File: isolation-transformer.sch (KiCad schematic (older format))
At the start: 0 parts

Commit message: Final schematic version
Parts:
- added CB1: 15A 250V, symbol Device:CircuitBreaker_1P
- added F1: 100°C, symbol Device:Fuse
- added FL1: JRT0406-2, symbol CustomParts:EMI_Filter_LL_CCC
- added J11: IEC 60320 C20, symbol Connector:Conn_01x03_Female
- added J12: CEE 7/3 Schuko, symbol Connector:Conn_01x03_Female
- added J13, J14: NEMA 5-15R, symbol Connector:Conn_01x03_Female
- added NE1, NE2, NE3: Lamp_Neon, symbol Device:Lamp_Neon
- added PS1: 12V 330mA, symbol Converter_ACDC:HLK-PM12
- added R14: 300R 200W, symbol Device:R
- added R15, R16, R17: 150K, symbol Device:R
- added SW1: 15A 250V, symbol CustomParts:SW_DPDT_x2_MSM
- added SW2, SW3: 6A 250V, symbol Switch:SW_SPST
- added TR1: 2600 VA, symbol Transformer:TRANSF6
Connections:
- new net: F1.2, TR1.2
- new net: F1.1, TR1.3
- new net: FL1.1, J11.3 (Pin_3), TR1.4
- new net: CB1.1, J11.1 (Pin_1)
- new net: CB1.2, SW1.2 (B), SW1.5 (B)
- new net: NE1.1, R15.1
- new net: FL1.3, PS1.1 (AC/L)
- new net: FL1.4, PS1.2 (AC/N)
- new net: FL1.2, SW1.4 (A)
- new net: J12.2 (Pin_2), J13.2 (Pin_2), J14.2 (Pin_2), SW3.1 (A)
- new net: NE2.1, R16.1
- new net: NE3.1, R17.1
- new net +12V: PS1.4 (+Vout)
- new net GND: FL1.5, J11.2 (Pin_2), PS1.3 (-Vout), SW2.2 (B), SW3.2 (B)
- new net Mode Selection/115V_1_L: J13.1 (Pin_1), NE2.2
- new net Mode Selection/115V_1_N: J13.3 (Pin_3), R16.2
- new net Mode Selection/115V_2_L: J14.1 (Pin_1), NE3.2
- new net Mode Selection/115V_2_N: J14.3 (Pin_3), R17.2
- new net Mode Selection/230V_L: J12.1 (Pin_1), NE1.2
- new net Mode Selection/230V_N: J12.3 (Pin_3), R15.2
- new net Mode Selection/MODE_SW: SW2.1 (A)
- new net Mode Selection/W5: TR1.5
- new net Mode Selection/W6: TR1.6
- new net Mode Selection/W7: TR1.7
- new net Mode Selection/W8: TR1.8
- new net Soft Start/BALLAST_1: R14.2
- new net Soft Start/BALLAST_2: R14.1
- new net Soft Start/PWR_1: SW1.1 (A)
- new net Soft Start/PWR_2: SW1.3 (C), TR1.1
- no-connect marks 0 -> 1
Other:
- note added: "Connect/disconnect\nprotective earth"
- note added: "Fuse TC-coupled to\nthe side of transformer"
- note added: "Goes to Soft Start\nand Mode Selection"
- note added: "In direct mode without\npower 230V mode is default"
- note added: "Toggle between\n230V/115V modes"
- note added: "Toggle between\nsoft-start/direct modes"

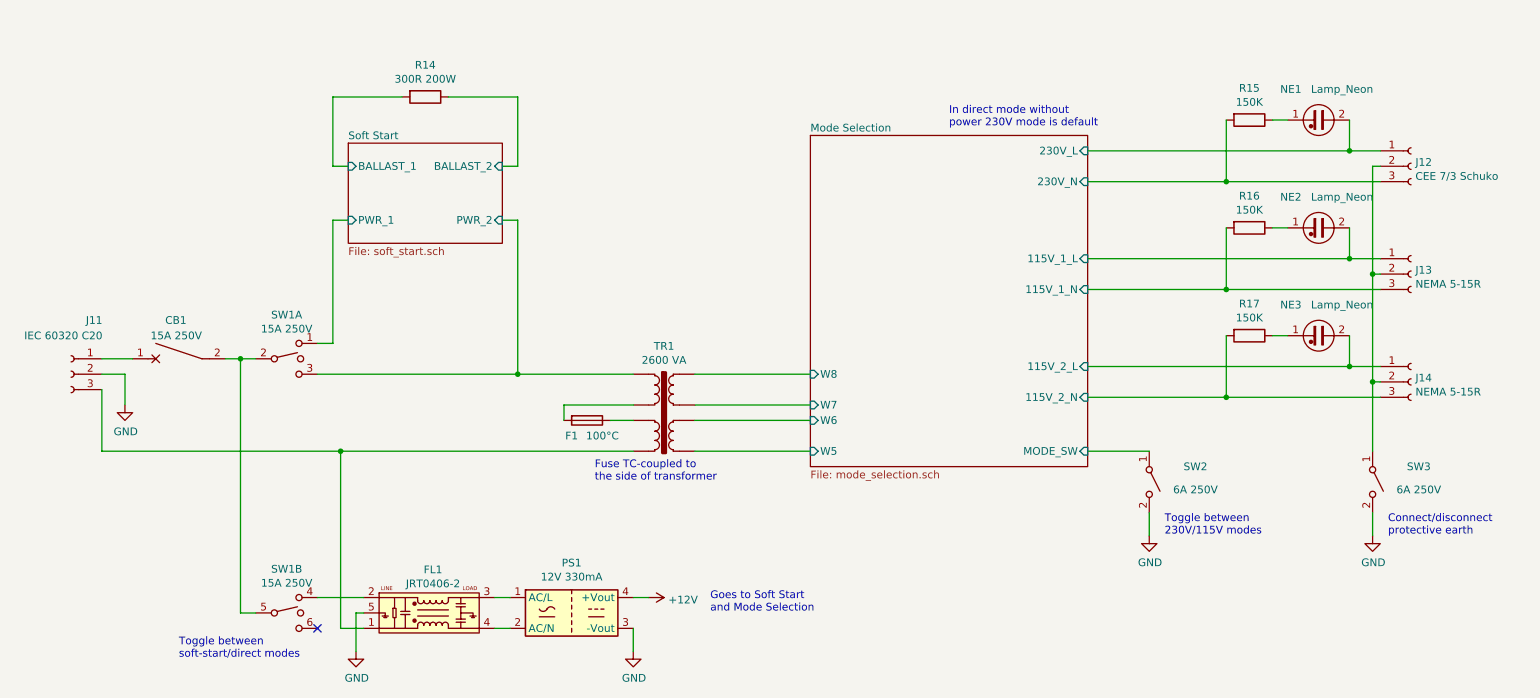
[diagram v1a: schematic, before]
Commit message: Actually used parts instead of generic ones
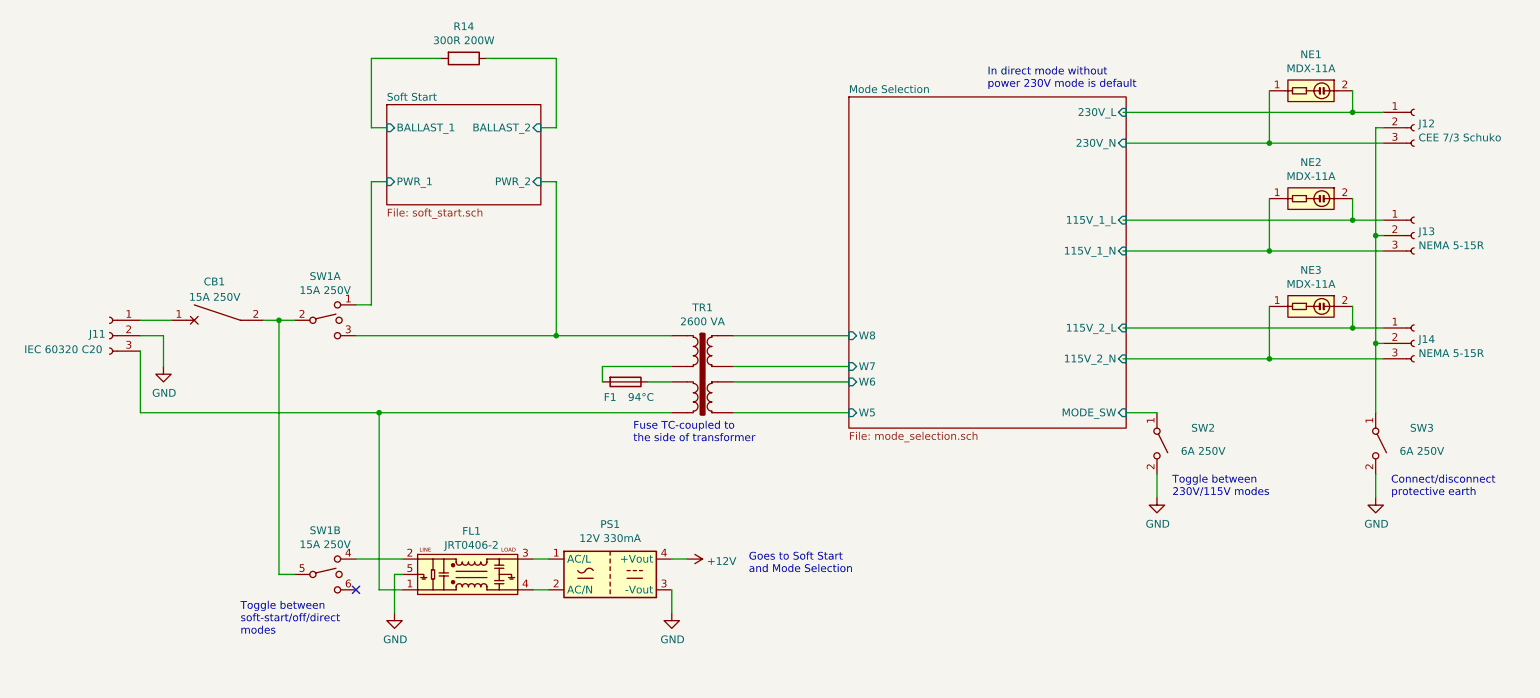
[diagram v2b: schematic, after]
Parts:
- removed NE1, NE2, NE3: Lamp_Neon, symbol Device:Lamp_Neon
- removed R15, R16, R17: 150K, symbol Device:R
- added NE1, NE2, NE3: MDX-11A, symbol CustomParts:Neon_Indicator
- F1: value 100°C -> 94°C
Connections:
- wire segments 69 -> 66
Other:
- note added: "Toggle between\nsoft-start/off/direct\nmodes"
- note removed: "Toggle between\nsoft-start/direct modes"
- moved on the sheet: CB1, F1, FL1, J11, J12, J13, J14, PS1, R14, SW1A, SW1B, SW2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

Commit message: Readme corrections, photos
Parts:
- added F1: 94°C, symbol Device:Fuse
- renumbered F1 to F2
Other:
- note added: "Fuses TC-coupled to\nthe sides of transformer"
- note removed: "Fuse TC-coupled to\nthe side of transformer"
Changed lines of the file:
@@
 $EndComp
 $Comp
-L Device:Fuse F1
+L Device:Fuse F2
 U 1 1 5D954501
 P 4900 3800
-F 0 "F1" V 5000 3700 50  0000 C CNN
+F 0 "F2" V 5000 3700 50  0000 C CNN
 F 1 "94°C" V 5000 3900 50  0000 C CNN
 F 2 "" V 4830 3800 50  0001 C CNN
@@
 	5050 3800 5200 3800
 Wire Wire Line
-	5200 3700 4750 3700
+	5200 3700 5050 3700
 Text Notes 7250 1900 0    50   ~ 0
 In direct mode without\npower 230V mode is default
@@
 Connect/disconnect\nprotective earth
 Text Notes 4950 4200 0    50   ~ 0
-Fuse TC-coupled to\nthe side of transformer
+Fuses TC-coupled to\nthe sides of transformer
 Text Notes 5700 5050 0    50   ~ 0
 Goes to Soft Start\nand Mode Selection
@@
 Connection ~ 9620 3450
 Connection ~ 9080 3650
+$Comp
+L Device:Fuse F1
+U 1 1 5D9FBBF9
+P 4900 3700
+F 0 "F1" V 4810 3600 50  0000 C CNN
+F 1 "94°C" V 4810 3800 50  0000 C CNN
+F 2 "" V 4830 3700 50  0001 C CNN
+F 3 "~" H 4900 3700 50  0001 C CNN
+	1    4900 3700
+	0    1    1    0
+$EndComp
 $EndSCHEMATC
